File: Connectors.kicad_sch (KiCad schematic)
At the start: 4 parts, among them J1 Conn_01x04_Pin, J2 Conn_01x04_Pin, J3 Conn_01x09_Socket, J4 Conn_02x03_Odd_Even

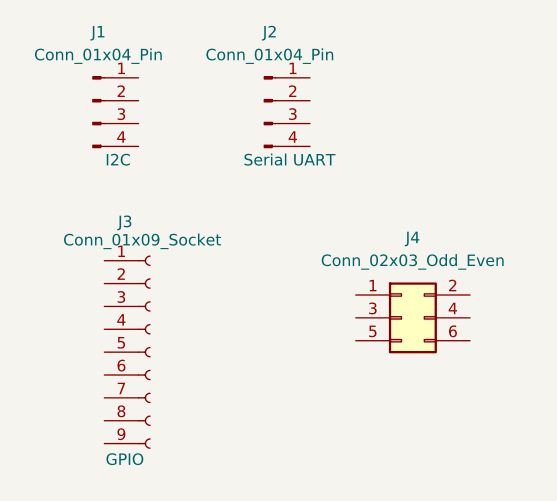
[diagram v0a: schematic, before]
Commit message: Added footprints to most of the symbols
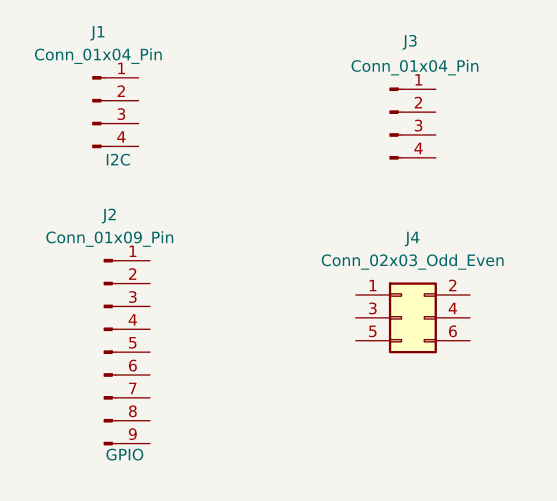
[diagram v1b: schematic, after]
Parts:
- removed J2: Conn_01x04_Pin, symbol Connector:Conn_01x04_Pin
- removed J3: Conn_01x09_Socket, symbol Connector:Conn_01x09_Socket
- added J2: Conn_01x09_Pin, Connector_PinHeader_2.54mm:PinHeader_1x09_P2.54mm_Vertical, symbol Connector:Conn_01x09_Pin
- added J3: Conn_01x04_Pin, Connector_PinHeader_2.54mm:PinHeader_1x04_P2.54mm_Vertical, symbol Connector:Conn_01x04_Pin
- J1: footprint (none) -> Connector_PinHeader_2.54mm:PinHeader_1x04_P2.54mm_Vertical
- J4: footprint (none) -> Connector_PinHeader_2.54mm:PinHeader_2x03_P2.54mm_Vertical
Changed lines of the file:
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@@
 			)
 		)
-		(property "Footprint" ""
+		(property "Footprint" "Connector_PinHeader_2.54mm:PinHeader_1x04_P2.54mm_Vertical"
 			(at 113.03 80.01 0)
 			(hide yes)
@@
 	)
 	(symbol
-		(lib_id "Connector:Conn_01x09_Socket")
-		(at 119.38 107.95 0)
+		(lib_id "Connector:Conn_01x04_Pin")
+		(at 146.05 81.28 0)
 		(unit 1)
 		(body_style 1)
@@
 		(dnp no)
 		(property "Reference" "J3"
-			(at 115.824 93.472 0)
-			(show_name no)
-			(do_not_autoplace no)
-			(effects
-				(font
-					(size 1.27 1.27)
-				)
-				(justify left)
-			)
-		)
-		(property "Value" "Conn_01x09_Socket"
-			(at 109.728 95.504 0)
-			(show_name no)
-			(do_not_autoplace no)
-			(effects
-				(font
-					(size 1.27 1.27)
-				)
-				(justify left)
-			)
-		)
-		(property "Footprint" ""
-			(at 119.38 107.95 0)
+			(at 148.336 73.406 0)
+			(show_name no)
+			(do_not_autoplace no)
+			(effects
+				(font
+					(size 1.27 1.27)
+				)
+			)
+		)
+		(property "Value" "Conn_01x04_Pin"
+			(at 148.844 76.2 0)
+			(show_name no)
+			(do_not_autoplace no)
+			(effects
+				(font
+					(size 1.27 1.27)
+				)
+			)
+		)
+		(property "Footprint" "Connector_PinHeader_2.54mm:PinHeader_1x04_P2.54mm_Vertical"
+			(at 146.05 81.28 0)
 			(hide yes)
 			(show_name no)
@@
 		)
 		(property "Datasheet" ""
-			(at 119.38 107.95 0)
-			(hide yes)
-			(show_name no)
-			(do_not_autoplace no)
-			(effects
-				(font
-					(size 1.27 1.27)
-				)
-			)
-		)
-		(property "Description" "Generic connector, single row, 01x09, script generated"
-			(at 119.38 107.95 0)
-			(hide yes)
-			(show_name no)
-			(do_not_autoplace no)
-			(effects
-				(font
-					(size 1.27 1.27)
-				)
-			)
-		)
-		(property "Purpose" "GPIO"
-			(at 116.586 119.888 0)
-			(show_name no)
-			(do_not_autoplace no)
-			(effects
-				(font
-					(size 1.27 1.27)
-				)
-			)
-		)
-		(pin "9"
-		)
-		(pin "8"
-		)
-		(pin "6"
-		)
-		(pin "7"
+			(at 146.05 81.28 0)
+			(hide yes)
+			(show_name no)
+			(do_not_autoplace no)
+			(effects
+				(font
+					(size 1.27 1.27)
+				)
+			)
+		)
+		(property "Description" "Generic connector, single row, 01x04, script generated"
+			(at 146.05 81.28 0)
+			(hide yes)
+			(show_name no)
+			(do_not_autoplace no)
+			(effects
+				(font
+					(size 1.27 1.27)
+				)
+			)
+		)
+		(pin "1"
+		)
+		(pin "4"
+		)
+		(pin "3"
 		)
 		(pin "2"
-		)
-		(pin "3"
-		)
-		(pin "4"
-		)
-		(pin "5"
-		)
-		(pin "1"
 		)
 		(instances
@@
 	)
 	(symbol
-		(lib_id "Connector:Conn_01x04_Pin")
-		(at 132.08 80.01 0)
+		(lib_id "Connector:Conn_01x09_Pin")
+		(at 114.3 107.95 0)
 		(unit 1)
 		(body_style 1)
@@
 		(dnp no)
 		(property "Reference" "J2"
-			(at 132.715 72.39 0)
-			(show_name no)
-			(do_not_autoplace no)
-			(effects
-				(font
-					(size 1.27 1.27)
-				)
-			)
-		)
-		(property "Value" "Conn_01x04_Pin"
-			(at 132.715 74.93 0)
-			(show_name no)
-			(do_not_autoplace no)
-			(effects
-				(font
-					(size 1.27 1.27)
-				)
-			)
-		)
-		(property "Footprint" ""
-			(at 132.08 80.01 0)
+			(at 114.935 92.71 0)
+			(show_name no)
+			(do_not_autoplace no)
+			(effects
+				(font
+					(size 1.27 1.27)
+				)
+			)
+		)
+		(property "Value" "Conn_01x09_Pin"
+			(at 114.935 95.25 0)
+			(show_name no)
+			(do_not_autoplace no)
+			(effects
+				(font
+					(size 1.27 1.27)
+				)
+			)
+		)
+		(property "Footprint" "Connector_PinHeader_2.54mm:PinHeader_1x09_P2.54mm_Vertical"
+			(at 114.3 107.95 0)
 			(hide yes)
 			(show_name no)
@@
 		)
 		(property "Datasheet" ""
-			(at 132.08 80.01 0)
-			(hide yes)
-			(show_name no)
-			(do_not_autoplace no)
-			(effects
-				(font
-					(size 1.27 1.27)
-				)
-			)
-		)
-		(property "Description" "Generic connector, single row, 01x04, script generated"
-			(at 132.08 80.01 0)
-			(hide yes)
-			(show_name no)
-			(do_not_autoplace no)
-			(effects
-				(font
-					(size 1.27 1.27)
-				)
-			)
-		)
-		(property "Purpose" "Serial UART"
-			(at 134.874 86.614 0)
-			(show_name no)
-			(do_not_autoplace no)
-			(effects
-				(font
-					(size 1.27 1.27)
-				)
-			)
+			(at 114.3 107.95 0)
+			(hide yes)
+			(show_name no)
+			(do_not_autoplace no)
+			(effects
+				(font
+					(size 1.27 1.27)
+				)
+			)
+		)
+		(property "Description" "Generic connector, single row, 01x09, script generated"
+			(at 114.3 107.95 0)
+			(hide yes)
+			(show_name no)
+			(do_not_autoplace no)
+			(effects
+				(font
+					(size 1.27 1.27)
+				)
+			)
+		)
+		(property "Purpose" "GPIO"
+			(at 116.586 119.38 0)
+			(show_name no)
+			(do_not_autoplace no)
+			(effects
+				(font
+					(size 1.27 1.27)
+				)
+			)
+		)
+		(pin "9"
+		)
+		(pin "8"
+		)
+		(pin "4"
+		)
+		(pin "1"
+		)
+		(pin "6"
+		)
+		(pin "7"
+		)
+		(pin "5"
+		)
+		(pin "3"
 		)
 		(pin "2"
-		)
-		(pin "1"
-		)
-		(pin "3"
-		)
-		(pin "4"
 		)
 		(instances
@@
 			)
 		)
-		(property "Footprint" ""
+		(property "Footprint" "Connector_PinHeader_2.54mm:PinHeader_2x03_P2.54mm_Vertical"
 			(at 147.32 104.14 0)
 			(hide yes)

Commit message: Both sheets wired but Vcc in sheet 2 is not connected. Maybe some issue with Kicad mismatch
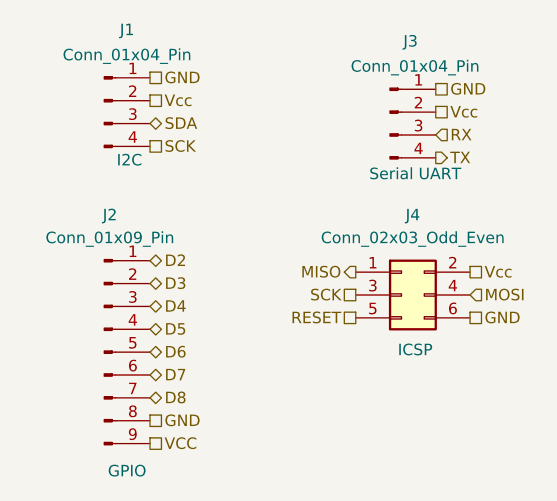
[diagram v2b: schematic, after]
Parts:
- J3: Purpose (none) -> Serial UART
- J4: Purpose (none) -> ICSP
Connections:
- net GND: now reaches J1.1 (Pin_1)
- net GND: now also J2.8 (Pin_8), J3.1 (Pin_1), J4.6 (Pin_6)
- net Vcc: now reaches J1.2 (Pin_2)
- net Vcc: now also J3.2 (Pin_2), J4.2 (Pin_2)
- net SDA: now reaches J1.3 (Pin_3)
- net SCK: now reaches J1.4 (Pin_4)
- net SCK: now also J4.3 (Pin_3)
- net RX: now reaches J3.3 (Pin_3)
- net TX: now reaches J3.4 (Pin_4)
- net D2: now reaches J2.1 (Pin_1)
- net D3: now reaches J2.2 (Pin_2)
- net D4: now reaches J2.3 (Pin_3)
- net D5: now reaches J2.4 (Pin_4)
- net D6: now reaches J2.5 (Pin_5)
- net D7: now reaches J2.6 (Pin_6)
- net D8: now reaches J2.7 (Pin_7)
- net VCC: now reaches J2.9 (Pin_9)
- net MISO: now reaches J4.1 (Pin_1)
- net MOSI: now reaches J4.4 (Pin_4)
- net RESET: now reaches J4.5 (Pin_5)
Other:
- moved on the sheet: J1, J4

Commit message: Fixed the Erc pin not connected caused by capitalization error VCC vs Vcc
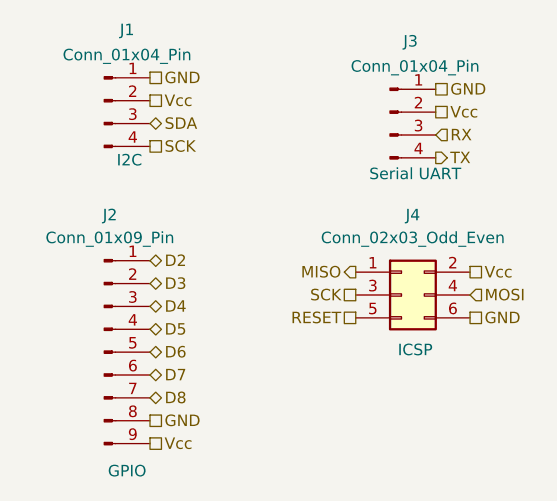
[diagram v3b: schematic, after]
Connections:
- net VCC is gone; now on net Vcc: J2.9 (Pin_9)
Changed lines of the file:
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@@
 		)
 	)
-	(hierarchical_label "VCC"
+	(hierarchical_label "Vcc"
 		(shape passive)
 		(at 119.38 118.11 0)

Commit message: fixed shematic errors SCL vs SCK
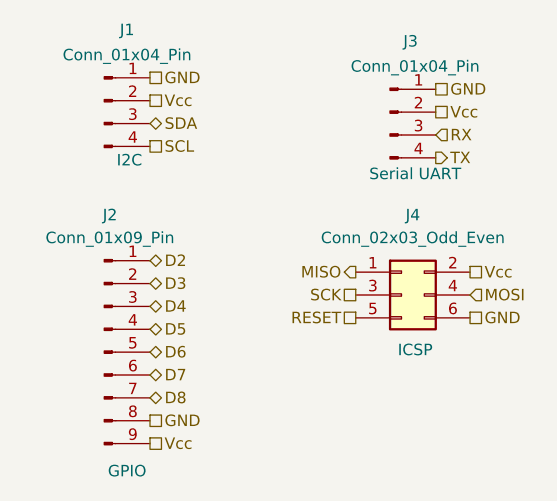
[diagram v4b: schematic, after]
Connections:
- net SCK: no longer J1.4 (Pin_4)
- new net SCL: J1.4 (Pin_4)
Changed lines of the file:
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@@
 		)
 	)
-	(hierarchical_label "SCK"
+	(hierarchical_label "SCL"
 		(shape passive)
 		(at 119.38 85.09 0)
